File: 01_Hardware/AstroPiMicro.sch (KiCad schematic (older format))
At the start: 41 parts, among them J1 RPi Connector, J10 CON_JOY_A, J2 USB_C_Receptacle_USB2.0, J3 Battery, J4 I2C_IMU, J5 DEBUG, J6 TFT_LCD, J7 CON_SW_A, J8 CON_SW_B, J9 CON_JOY_B, SW1 SW_SPDT, U1 LM809, U2 STM32G431KBTx, U3 MCP73831-2-OT, U4 TPS61090, U5 SKRHAAE010, Y1 ABM3B-16MHz

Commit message: Finished board outline
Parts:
- J3: footprint Connector_JST:JST_PH_S2B-PH-K_1x02_P2.00mm_Horizontal -> Connector_JST:JST_PH_S2B-PH-SM4-TB_1x02-1MP_P2.00mm_Horizontal
- J6: footprint Connector_JST:JST_PH_S11B-PH-K_1x11_P2.00mm_Horizontal -> Connector_JST:JST_PH_B11B-PH-K_1x11_P2.00mm_Vertical
- J8: footprint Connector_JST:JST_PH_B3B-PH-K_1x03_P2.00mm_Vertical -> Connector_JST:JST_PH_B3B-PH-SM4-TB_1x03-1MP_P2.00mm_Vertical
- J9: footprint Connector_JST:JST_PH_B6B-PH-K_1x06_P2.00mm_Vertical -> Connector_JST:JST_PH_B6B-PH-SM4-TB_1x06-1MP_P2.00mm_Vertical
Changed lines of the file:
@@
 F 0 "J6" H 10455 5017 50  0000 L CNN
 F 1 "TFT_LCD" H 10455 4926 50  0000 L CNN
-F 2 "Connector_JST:JST_PH_S11B-PH-K_1x11_P2.00mm_Horizontal" H 10375 4975 50  0001 C CNN
+F 2 "Connector_JST:JST_PH_B11B-PH-K_1x11_P2.00mm_Vertical" H 10375 4975 50  0001 C CNN
 F 3 "~" H 10375 4975 50  0001 C CNN
 	1    10375 4975
@@
 F 0 "J3" H 5830 4542 50  0000 L CNN
 F 1 "Battery" H 5830 4451 50  0000 L CNN
-F 2 "Connector_JST:JST_PH_S2B-PH-K_1x02_P2.00mm_Horizontal" H 5750 4550 50  0001 C CNN
+F 2 "Connector_JST:JST_PH_S2B-PH-SM4-TB_1x02-1MP_P2.00mm_Horizontal" H 5750 4550 50  0001 C CNN
 F 3 "~" H 5750 4550 50  0001 C CNN
 	1    5750 4550
@@
 F 0 "J9" H 7605 2867 50  0000 L CNN
 F 1 "CON_JOY_B" H 7605 2776 50  0000 L CNN
-F 2 "Connector_JST:JST_PH_B6B-PH-K_1x06_P2.00mm_Vertical" H 7525 2875 50  0001 C CNN
+F 2 "Connector_JST:JST_PH_B6B-PH-SM4-TB_1x06-1MP_P2.00mm_Vertical" H 7525 2875 50  0001 C CNN
 F 3 "~" H 7525 2875 50  0001 C CNN
 	1    7525 2875
@@
 F 0 "J8" H 4755 7292 50  0000 L CNN
 F 1 "CON_SW_B" H 4755 7201 50  0000 L CNN
-F 2 "Connector_JST:JST_PH_B3B-PH-K_1x03_P2.00mm_Vertical" H 4675 7250 50  0001 C CNN
+F 2 "Connector_JST:JST_PH_B3B-PH-SM4-TB_1x03-1MP_P2.00mm_Vertical" H 4675 7250 50  0001 C CNN
 F 3 "~" H 4675 7250 50  0001 C CNN
 	1    4675 7250

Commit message: Routing finished.
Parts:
- removed C3: 100uF, Capacitor_Tantalum_SMD:CP_EIA-7343-31_Kemet-D_Pad2.25x2.55mm_HandSolder, symbol Device:CP_Small
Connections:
- net +BATT: now also U4.10 (SYNC)
- net GND: no longer U4.10 (SYNC)
- net ~LOW_BAT: now also J1.12 (Pin_12); no longer J1.37 (Pin_37)
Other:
- note added: "- 10uF input capacitor is maximum tolerated by USB specification"
- note added: "- All Joystick GPIOs & ~LOW_BAT~ have internal pull-up resistors!"
- note removed: "All Joystick GPIOs & ~LOW_BAT~ have internal pull-up resistors!"
- moved on the sheet: C5
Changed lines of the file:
@@
 $EndComp
 Connection ~ 6025 1475
-Wire Wire Line
-	6025 1675 6475 1675
 $Comp
 L Regulator_Switching:TPS61090 U?
@@
 Text Label 7650 1475 2    50   ~ 0
 ~LOW_BAT
-Text Label 9625 2700 0    50   ~ 0
-~LOW_BAT
 Text Notes 1925 900  0    50   ~ 0
 Reset circuit
-$Comp
-L Device:CP_Small C3
-U 1 1 5EBB2A9A
-P 1900 4725
-F 0 "C3" H 1988 4771 50  0000 L CNN
-F 1 "100uF" H 1988 4680 50  0000 L CNN
-F 2 "Capacitor_Tantalum_SMD:CP_EIA-7343-31_Kemet-D_Pad2.25x2.55mm_HandSolder" H 1900 4725 50  0001 C CNN
-F 3 "T495D107K010ATE100" H 1900 4725 50  0001 C CNN
-	1    1900 4725
-	1    0    0    -1
-$EndComp
-$Comp
-L power:VBUS #PWR0134
-U 1 1 5EBB3808
-P 1900 4625
-F 0 "#PWR0134" H 1900 4475 50  0001 C CNN
-F 1 "VBUS" H 1915 4798 50  0000 C CNN
-F 2 "" H 1900 4625 50  0001 C CNN
-F 3 "" H 1900 4625 50  0001 C CNN
-	1    1900 4625
-	1    0    0    -1
-$EndComp
-$Comp
-L power:GND #PWR0135
-U 1 1 5EBB3C57
-P 1900 4825
-F 0 "#PWR0135" H 1900 4575 50  0001 C CNN
-F 1 "GND" H 2025 4725 50  0000 C CNN
-F 2 "" H 1900 4825 50  0001 C CNN
-F 3 "" H 1900 4825 50  0001 C CNN
-	1    1900 4825
-	1    0    0    -1
-$EndComp
 $Comp
 L power:+5V #PWR0136
@@
 Text Label 10850 2100 2    50   ~ 0
 LCD_~TCS
-Wire Wire Line
-	9625 2700 10000 2700
 Text Label 10925 1200 2    50   ~ 0
 PI_UART_TX
@@
 NoConn ~ 10500 2400
 NoConn ~ 10500 2200
-NoConn ~ 10500 2000
 NoConn ~ 10500 1900
 NoConn ~ 10500 1700
-NoConn ~ 10500 1400
 NoConn ~ 10000 1100
 NoConn ~ 10000 1000
@@
 L power:GND #PWR0139
 U 1 1 5EB6BD8F
-P 3925 5050
+P 2125 4825
 AR Path="/5EB6BD8F" Ref="#PWR0139"  Part="1"
 AR Path="/5EB95111/5EB6BD8F" Ref="#PWR?"  Part="1"
-F 0 "#PWR0139" H 3925 4800 50  0001 C CNN
-F 1 "GND" H 3930 4877 50  0000 C CNN
-F 2 "" H 3925 5050 50  0001 C CNN
-F 3 "" H 3925 5050 50  0001 C CNN
-	1    3925 5050
+F 0 "#PWR0139" H 2125 4575 50  0001 C CNN
+F 1 "GND" H 2130 4652 50  0000 C CNN
+F 2 "" H 2125 4825 50  0001 C CNN
+F 3 "" H 2125 4825 50  0001 C CNN
+	1    2125 4825
 	1    0    0    -1
 $EndComp
@@
 L Device:C_Small C5
 U 1 1 5EB6BD89
-P 3925 4950
+P 2125 4725
 AR Path="/5EB6BD89" Ref="C5"  Part="1"
 AR Path="/5EB95111/5EB6BD89" Ref="C?"  Part="1"
-F 0 "C5" H 4017 4996 50  0000 L CNN
-F 1 "10uF" H 4017 4905 50  0000 L CNN
-F 2 "Capacitor_SMD:C_0805_2012Metric" H 3925 4950 50  0001 C CNN
-F 3 "~" H 3925 4950 50  0001 C CNN
-	1    3925 4950
+F 0 "C5" H 2217 4771 50  0000 L CNN
+F 1 "10uF" H 2217 4680 50  0000 L CNN
+F 2 "Capacitor_SMD:C_0805_2012Metric" H 2125 4725 50  0001 C CNN
+F 3 "~" H 2125 4725 50  0001 C CNN
+	1    2125 4725
 	1    0    0    -1
 $EndComp
@@
 L power:VBUS #PWR0140
 U 1 1 5EB6BD83
-P 3925 4850
+P 2125 4625
 AR Path="/5EB6BD83" Ref="#PWR0140"  Part="1"
 AR Path="/5EB95111/5EB6BD83" Ref="#PWR?"  Part="1"
-F 0 "#PWR0140" H 3925 4700 50  0001 C CNN
-F 1 "VBUS" H 3940 5023 50  0000 C CNN
-F 2 "" H 3925 4850 50  0001 C CNN
-F 3 "" H 3925 4850 50  0001 C CNN
-	1    3925 4850
+F 0 "#PWR0140" H 2125 4475 50  0001 C CNN
+F 1 "VBUS" H 2140 4798 50  0000 C CNN
+F 2 "" H 2125 4625 50  0001 C CNN
+F 3 "" H 2125 4625 50  0001 C CNN
+	1    2125 4625
 	1    0    0    -1
 $EndComp
@@
 Wire Wire Line
 	9625 1500 10000 1500
-Text Label 10925 1600 2    50   ~ 0
-GPIO23
-Wire Wire Line
-	10925 1600 10500 1600
 Wire Notes Line
 	5125 525  5125 4150
@@
 	7275 1475 7650 1475
 Text Notes 6675 5325 0    50   ~ 0
-All Joystick GPIOs & ~LOW_BAT~ have internal pull-up resistors!
+- All Joystick GPIOs & ~LOW_BAT~ have internal pull-up resistors!
 Text Notes 6675 5175 0    50   ~ 10
 Important Information
+Text Notes 6675 5425 0    50   ~ 0
+- 10uF input capacitor is maximum tolerated by USB specification
+Text Label 10925 1400 2    50   ~ 0
+~LOW_BAT
+NoConn ~ 10000 2700
+$Comp
+L power:+BATT #PWR?
+U 1 1 5EC81BCC
+P 6375 1675
+AR Path="/5EC81BCC" Ref="#PWR?"  Part="1"
+AR Path="/5EB95111/5EC81BCC" Ref="#PWR?"  Part="1"
+F 0 "#PWR?" H 6375 1525 50  0001 C CNN
+F 1 "+BATT" H 6250 1775 50  0000 C CNN
+F 2 "" H 6375 1675 50  0001 C CNN
+F 3 "" H 6375 1675 50  0001 C CNN
+	1    6375 1675
+	1    0    0    -1
+$EndComp
+Wire Wire Line
+	6475 1675 6375 1675
+NoConn ~ 10500 2000
+Wire Wire Line
+	10925 1600 10500 1600
+Text Label 10925 1600 2    50   ~ 0
+GPIO23
+Wire Wire Line
+	10500 1400 10925 1400
 $EndSCHEMATC

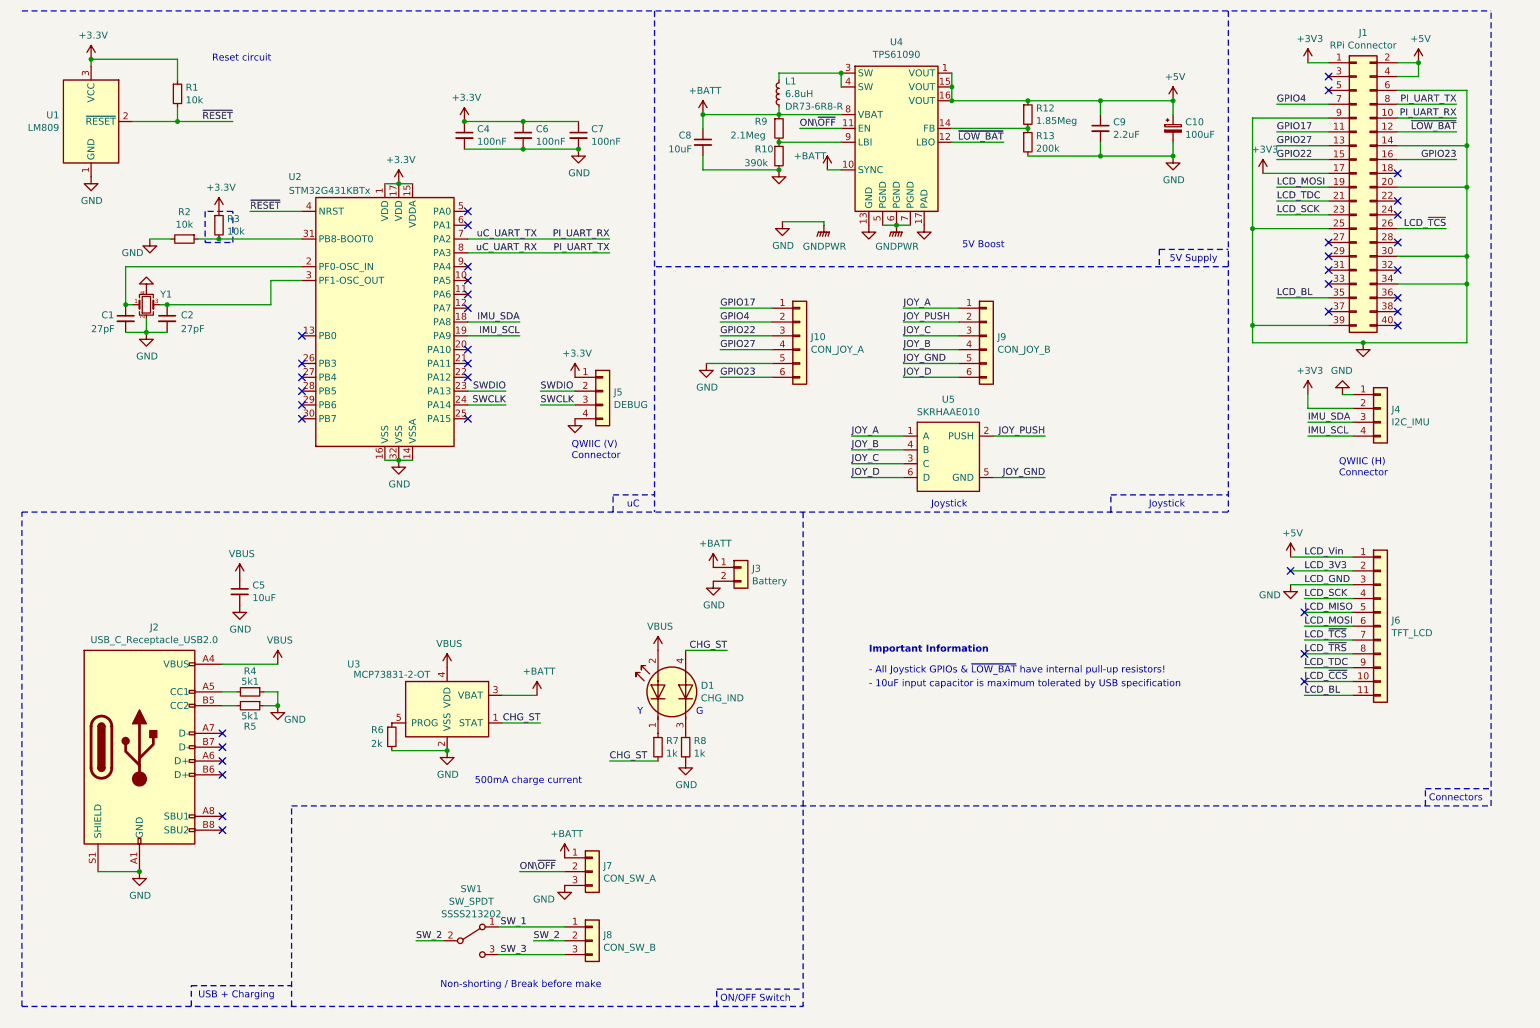
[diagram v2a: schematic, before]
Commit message: Almost all footprints have MFN now
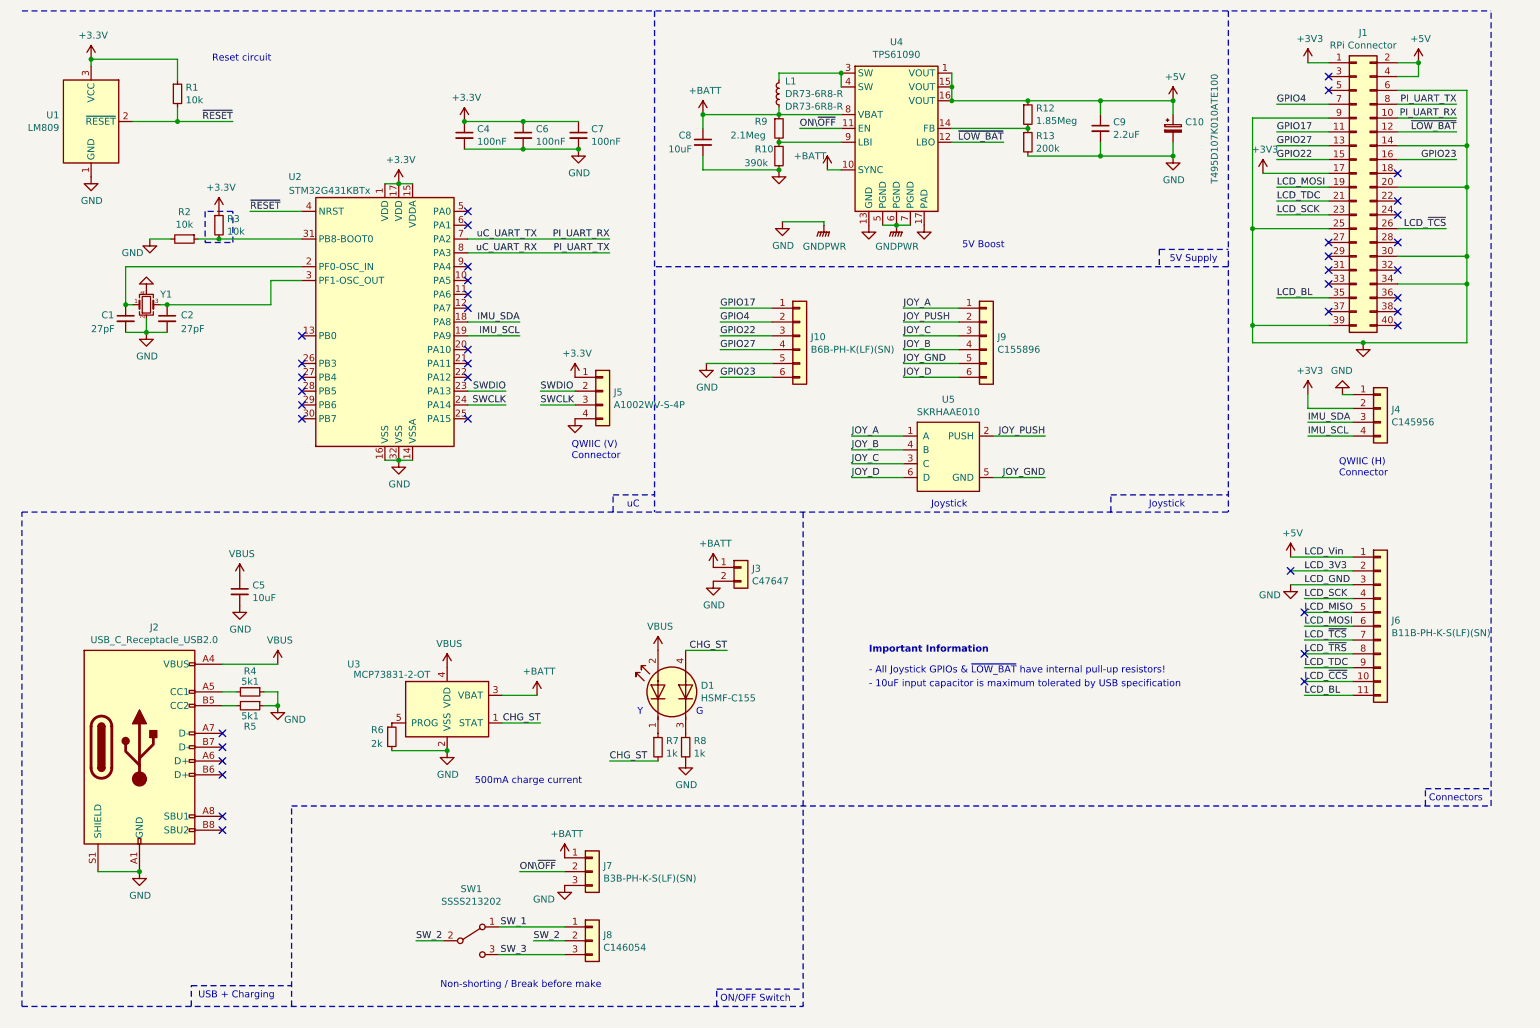
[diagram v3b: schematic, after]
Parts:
- C10: value 100uF -> T495D107K010ATE100
- D1: value CHG_IND -> HSMF-C155
- J10: value CON_JOY_A -> B6B-PH-K(LF)(SN)
- J3: value Battery -> C47647
- J4: value I2C_IMU -> C145956
- J5: value DEBUG -> A1002WV-S-4P
- J6: value TFT_LCD -> B11B-PH-K-S(LF)(SN)
- J7: value CON_SW_A -> B3B-PH-K-S(LF)(SN)
- J8: value CON_SW_B -> C146054
- J9: value CON_JOY_B -> C155896
- L1: value 6.8uH -> DR73-6R8-R
- SW1: value SW_SPDT -> SSSS213202
- Y1: value ABM3B-16MHz -> X1H016000FI1H-X
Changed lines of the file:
@@
 P 10375 3400
 F 0 "J4" H 10455 3392 50  0000 L CNN
-F 1 "I2C_IMU" H 10455 3301 50  0000 L CNN
+F 1 "C145956" H 10455 3301 50  0000 L CNN
 F 2 "Connector_JST:JST_SH_SM04B-SRSS-TB_1x04-1MP_P1.00mm_Horizontal" H 10375 3400 50  0001 C CNN
 F 3 "~" H 10375 3400 50  0001 C CNN
@@
 P 10375 4975
 F 0 "J6" H 10455 5017 50  0000 L CNN
-F 1 "TFT_LCD" H 10455 4926 50  0000 L CNN
+F 1 "B11B-PH-K-S(LF)(SN)" H 10455 4926 50  0000 L CNN
 F 2 "Connector_JST:JST_PH_B11B-PH-K_1x11_P2.00mm_Vertical" H 10375 4975 50  0001 C CNN
 F 3 "~" H 10375 4975 50  0001 C CNN
@@
 P 1450 2650
 F 0 "Y1" H 1550 2725 50  0000 L CNN
-F 1 "ABM3B-16MHz" H 1594 2605 50  0001 L CNN
+F 1 "X1H016000FI1H-X" H 1594 2605 50  0001 L CNN
 F 2 "Crystal:Crystal_SMD_Abracon_ABM3B-4Pin_5.0x3.2mm" H 1450 2650 50  0001 C CNN
 F 3 "~" H 1450 2650 50  0001 C CNN
@@
 P 4750 3275
 F 0 "J5" H 4830 3267 50  0000 L CNN
-F 1 "DEBUG" H 4830 3176 50  0000 L CNN
+F 1 "A1002WV-S-4P" H 4830 3176 50  0000 L CNN
 F 2 "Connector_JST:JST_SH_BM04B-SRSS-TB_1x04-1MP_P1.00mm_Vertical" H 4750 3275 50  0001 C CNN
 F 3 "~" H 4750 3275 50  0001 C CNN
@@
 AR Path="/5EB65329" Ref="L1"  Part="1"
 F 0 "L1" H 5981 1034 50  0000 R CNN
-F 1 "6.8uH" H 5981 1125 50  0000 R CNN
+F 1 "DR73-6R8-R" H 5981 1125 50  0000 R CNN
 F 2 "astropi:DR73" H 6025 1125 50  0001 C CNN
 F 3 "DR73-6R8-R" H 5981 1216 50  0000 R CNN
@@
 AR Path="/5EB65352" Ref="C10"  Part="1"
 F 0 "C10" H 8963 1421 50  0000 L CNN
-F 1 "100uF" H 8963 1330 50  0000 L CNN
+F 1 "T495D107K010ATE100" V 9175 975 50  0000 L CNN
 F 2 "Capacitor_Tantalum_SMD:CP_EIA-7343-31_Kemet-D_Pad2.25x2.55mm_HandSolder" H 8875 1375 50  0001 C CNN
 F 3 "T495D107K010ATE100" H 8875 1375 50  0001 C CNN
@@
 AR Path="/5EB6537E" Ref="J3"  Part="1"
 F 0 "J3" H 5830 4542 50  0000 L CNN
-F 1 "Battery" H 5830 4451 50  0000 L CNN
+F 1 "C47647" H 5830 4451 50  0000 L CNN
 F 2 "Connector_JST:JST_PH_S2B-PH-SM4-TB_1x02-1MP_P2.00mm_Horizontal" H 5750 4550 50  0001 C CNN
 F 3 "~" H 5750 4550 50  0001 C CNN
@@
 AR Path="/5EB95111/5EB6BD3E" Ref="D?"  Part="1"
 F 0 "D1" V 5296 5240 50  0000 R CNN
-F 1 "CHG_IND" V 5205 5240 50  0000 R CNN
+F 1 "HSMF-C155" V 5205 5240 50  0000 R CNN
 F 2 "LED_SMD:LED_Avago_PLCC4_3.2x2.8mm_CW" H 5280 5450 50  0001 C CNN
 F 3 "~" H 5280 5450 50  0001 C CNN
@@
 AR Path="/5EB65397" Ref="SW1"  Part="1"
 F 0 "SW1" H 3800 7625 50  0000 C CNN
-F 1 "SW_SPDT" H 3800 7534 50  0000 C CNN
+F 1 "SSSS213202" H 3800 7534 50  0000 C CNN
 F 2 "astropi:SSSS213202" H 3800 7250 50  0001 C CNN
-F 3 "SSSS213202" H 3800 7443 50  0000 C CNN
+F 3 "SSSS213202" H 3800 7443 50  0001 C CNN
 	1    3800 7250
 	1    0    0    -1
@@
 P 4675 6750
 F 0 "J7" H 4755 6792 50  0000 L CNN
-F 1 "CON_SW_A" H 4755 6701 50  0000 L CNN
+F 1 "B3B-PH-K-S(LF)(SN)" H 4755 6701 50  0000 L CNN
 F 2 "Connector_JST:JST_PH_B3B-PH-K_1x03_P2.00mm_Vertical" H 4675 6750 50  0001 C CNN
 F 3 "~" H 4675 6750 50  0001 C CNN
@@
 P 6175 2875
 F 0 "J10" H 6255 2867 50  0000 L CNN
-F 1 "CON_JOY_A" H 6255 2776 50  0000 L CNN
+F 1 "B6B-PH-K(LF)(SN)" H 6255 2776 50  0000 L CNN
 F 2 "Connector_JST:JST_PH_B6B-PH-K_1x06_P2.00mm_Vertical" H 6175 2875 50  0001 C CNN
 F 3 "~" H 6175 2875 50  0001 C CNN
@@
 P 7525 2875
 F 0 "J9" H 7605 2867 50  0000 L CNN
-F 1 "CON_JOY_B" H 7605 2776 50  0000 L CNN
+F 1 "C155896" H 7605 2776 50  0000 L CNN
 F 2 "Connector_JST:JST_PH_B6B-PH-SM4-TB_1x06-1MP_P2.00mm_Vertical" H 7525 2875 50  0001 C CNN
 F 3 "~" H 7525 2875 50  0001 C CNN
@@
 P 4675 7250
 F 0 "J8" H 4755 7292 50  0000 L CNN
-F 1 "CON_SW_B" H 4755 7201 50  0000 L CNN
+F 1 "C146054" H 4755 7201 50  0000 L CNN
 F 2 "Connector_JST:JST_PH_B3B-PH-SM4-TB_1x03-1MP_P2.00mm_Vertical" H 4675 7250 50  0001 C CNN
 F 3 "~" H 4675 7250 50  0001 C CNN
@@
 NoConn ~ 10000 2700
 $Comp
-L power:+BATT #PWR?
+L power:+BATT #PWR0130
 U 1 1 5EC81BCC
 P 6375 1675
-AR Path="/5EC81BCC" Ref="#PWR?"  Part="1"
+AR Path="/5EC81BCC" Ref="#PWR0130"  Part="1"
 AR Path="/5EB95111/5EC81BCC" Ref="#PWR?"  Part="1"
-F 0 "#PWR?" H 6375 1525 50  0001 C CNN
+F 0 "#PWR0130" H 6375 1525 50  0001 C CNN
 F 1 "+BATT" H 6250 1775 50  0000 C CNN
 F 2 "" H 6375 1675 50  0001 C CNN

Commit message: Finished BOM, PCB and ordered PCB
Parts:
- C1, C2: MPN (none) -> GRM1885C1H270JA01D
- C10: value T495D107K010ATE100 -> 100uF; MPN (none) -> T495D107K010ATE100
- C4, C6, C7: MPN (none) -> 0603B104K500AT
- C5, C8: MPN (none) -> C2012X5R1C106KTJ00E
- C9: MPN (none) -> CC0805KRX5R7BB225
- D1: value HSMF-C155 -> Status LED; MPN (none) -> HSMF-C155
- J10: value B6B-PH-K(LF)(SN) -> 6-pin JST PH; MPN (none) -> B6B-PH-K(LF)(SN)
- J3: value C47647 -> 2-pin JST PH; MPN (none) -> C47647
- J4: value C145956 -> 4-pin JST SH; MPN (none) -> C145956
- J5: value A1002WV-S-4P -> 4-pin JST SH; MPN (none) -> A1002WV-S-4P
- J6: value B11B-PH-K-S(LF)(SN) -> 11-pin JST PH; MPN (none) -> B11B-PH-K-S(LF)(SN)
- J7: value B3B-PH-K-S(LF)(SN) -> 3-pin JST PH; MPN (none) -> B3B-PH-K-S(LF)(SN)
- J8: value C146054 -> 3-pin JST PH; MPN (none) -> C146054
- J9: value C155896 -> 6-pin JST PH; MPN (none) -> C155896
- L1: value DR73-6R8-R -> 6.8uH; footprint astropi:DR73 -> Inductor_SMD:L_Taiyo-Yuden_NR-50xx_HandSoldering; MPN (none) -> NRS5040T6R8MMGJ
- R1, R2, R3: MPN (none) -> 0603WAJ0103T5E
- R10: MPN (none) -> RK73B1JTTD394J
- R12: MPN (none) -> 0603WAF1874T5E
- R13: MPN (none) -> 0603WAF2053T5E
- R4, R5: MPN (none) -> 0603WAF5101T5E
- R6: MPN (none) -> CR0603FA2001G
- R7, R8: MPN (none) -> 0603WAF1001T5E
- R9: value 2.1Meg -> 2.1M; MPN (none) -> RTT032104FTP
- SW1: value SSSS213202 -> SW-ON-OFF; MPN (none) -> SSSS213202
- U1: MPN (none) -> LM809M3-3.08/NOPB
- U2: MPN (none) -> STM32G431KBT8
- U3: MPN (none) -> MCP73831T-2ACI/OT
- U4: MPN (none) -> TPS61090RSAR
- U5: value SKRHAAE010 -> Joystick; MPN (none) -> SKRHAAE010
- Y1: value X1H016000FI1H-X -> 16MHz; MPN (none) -> X1H016000FI1H-X
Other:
- note removed: "5V Boost"
